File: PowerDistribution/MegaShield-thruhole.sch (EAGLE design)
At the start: 36 parts, among them IC1 TLE5205-2, IC2 TLE5205-2, IC3 TLE5205-2, J10 DCJ0202

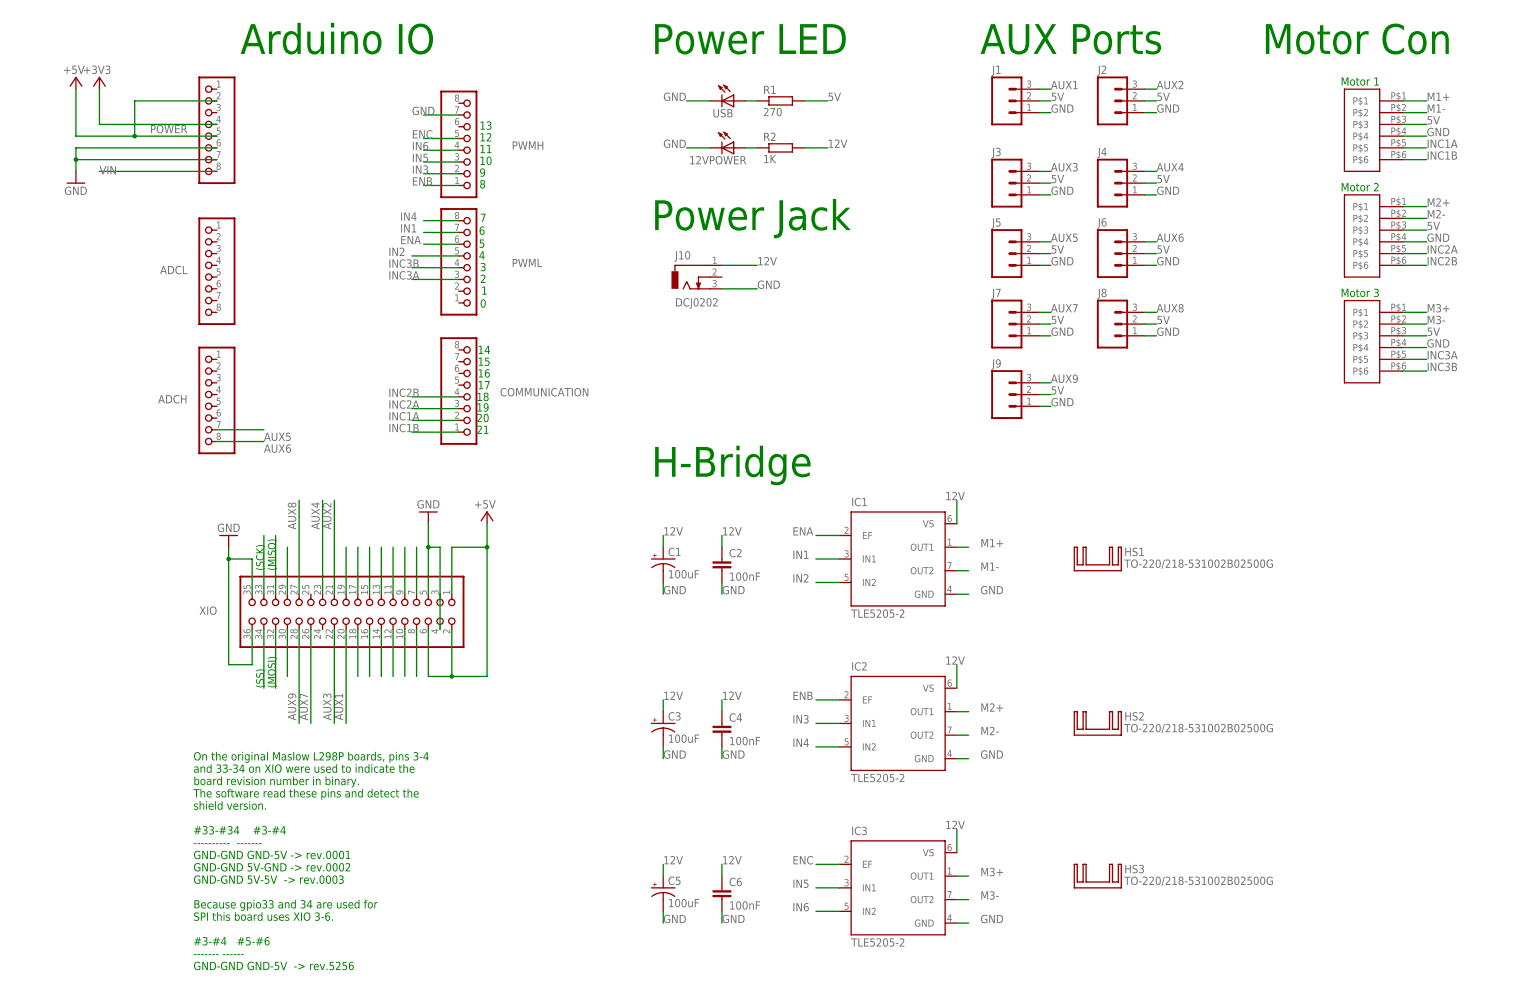
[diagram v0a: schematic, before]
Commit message: clean up and correct pin spacing
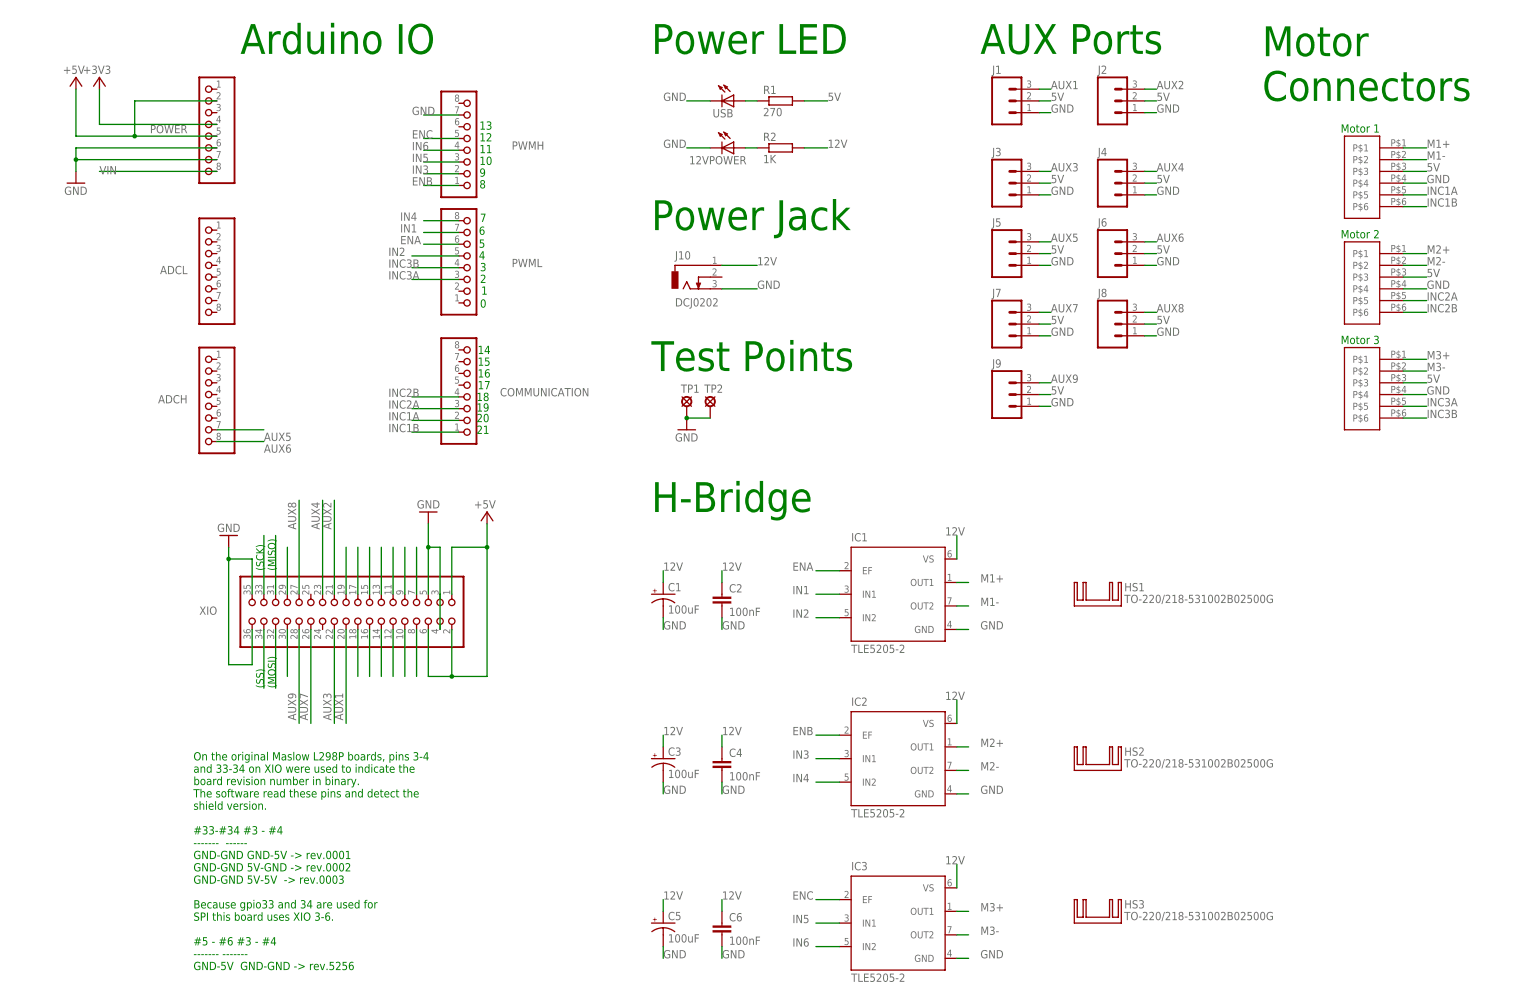
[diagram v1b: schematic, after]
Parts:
- added TP1, TP2: LSP10, solpad:LSP10
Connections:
- net GND: now also TP1.MP, TP2.MP
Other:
- note added: "Motor Connectors"
- note added: "On the original Maslow L298P boards, pins 3-4 and 33-34 on XIO were used to indicate the board revision number in binary. The software read these pins and detect the shield version. #33-#34 #3 - #4 ------- ------ GND-GND GND-5V -> rev.0001 GND-GND 5V-GND -> rev.0002 GND-GND 5V-5V -> rev.0003 Because gpio33 and 34 are used for SPI this board uses XIO 3-6. #5 - #6 #3 - #4 ------- ------- GND-5V GND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"
- note added: "Test Points"
- note removed: "Motor Con"
- note removed: "On the original Maslow L298P boards, pins 3-4 and 33-34 on XIO were used to indicate the board revision number in binary. The software read these pins and detect the shield version. #33-#34 #3-#4 ---------- ------- GND-GND GND-5V -> rev.0001 GND-GND 5V-GND -> rev.0002 GND-GND 5V-5V -> rev.0003 Because gpio33 and 34 are used for SPI this board uses XIO 3-6. #3-#4 #5-#6 ------- ------ GND-GND GND-5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"
- moved on the sheet: C1, C2, C3, C4, C5, C6, HS1, HS2, HS3, IC1, IC2, IC3

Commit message: Move AUX conections to other source pins
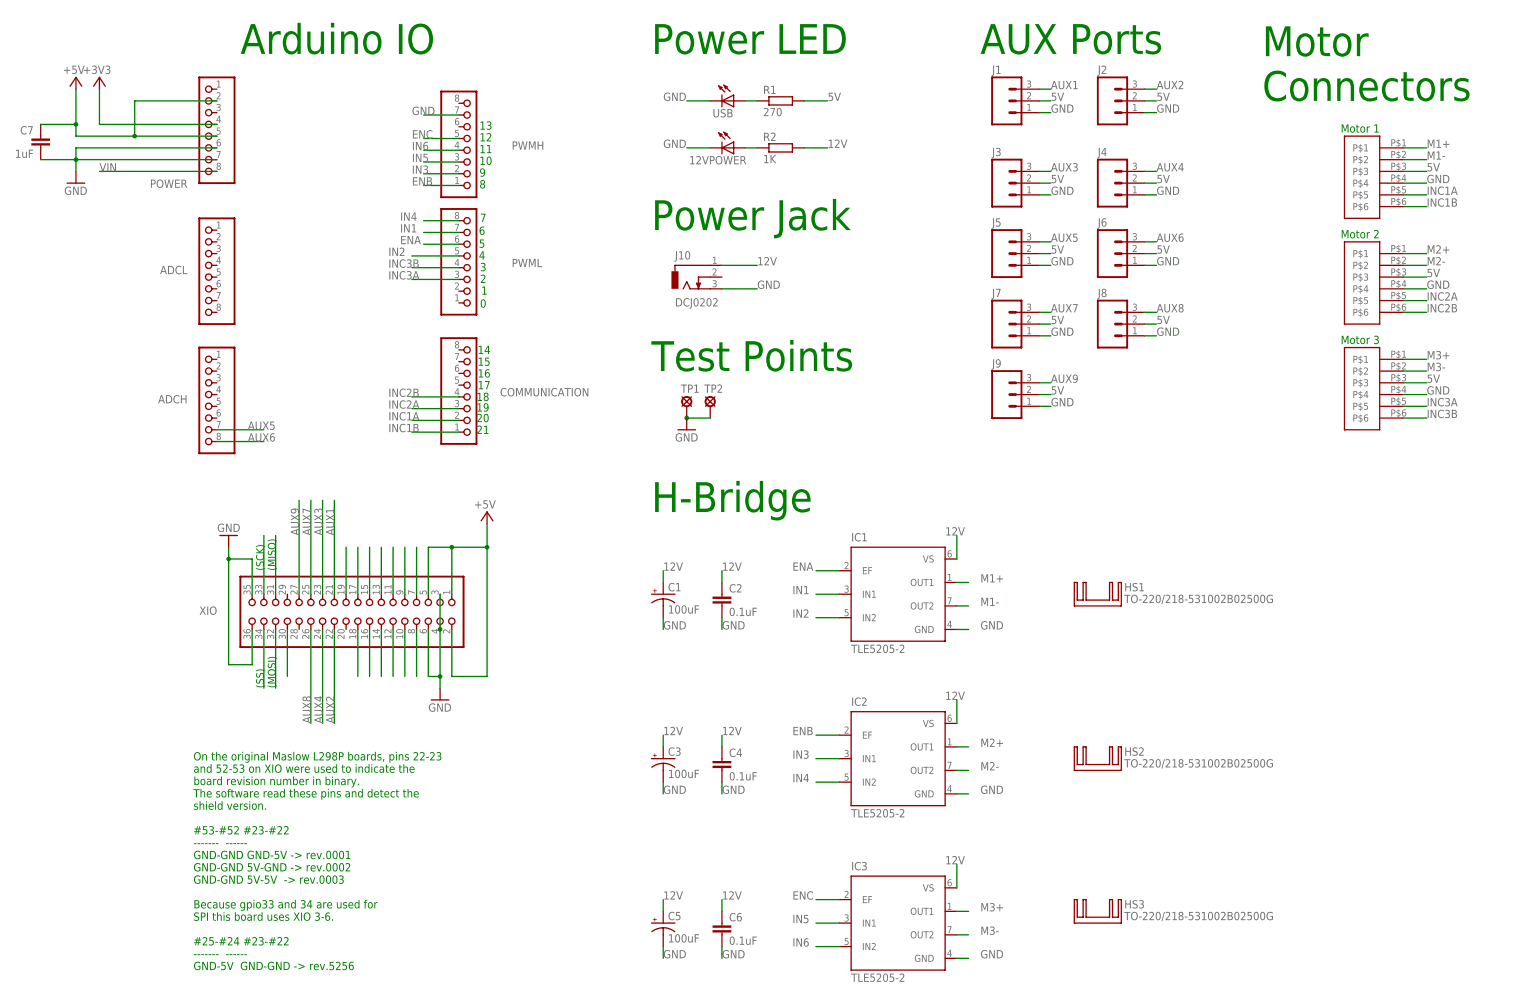
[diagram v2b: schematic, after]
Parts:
- added C7: 1uF, SparkFun:CAPPTH
- C2, C4, C6: value 100nF -> 0.1uF
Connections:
- removed net PL1: XIO.29
- net 5V: now also C7.1, XIO.5; no longer XIO.6
- net AUX1: now also XIO.21; no longer XIO.20
- net AUX2: now also XIO.22; no longer XIO.21
- net AUX3: now also XIO.23; no longer XIO.22
- net AUX4: now also XIO.24; no longer XIO.23
- net AUX7: now also XIO.25; no longer XIO.26
- net AUX8: now also XIO.26; no longer XIO.27
- net AUX9: now also XIO.27; no longer XIO.28
- net GND: now also C7.2, XIO.6; no longer XIO.5
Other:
- note added: "On the original Maslow L298P boards, pins 22-23 and 52-53 on XIO were used to indicate the board revision number in binary. The software read these pins and detect the shield version. #53-#52 #23-#22 ------- ------ GND-GND GND-5V -> rev.0001 GND-GND 5V-GND -> rev.0002 GND-GND 5V-5V -> rev.0003 Because gpio33 and 34 are used for SPI this board uses XIO 3-6. #25-#24 #23-#22 ------- ------ GND-5V GN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"
- note removed: "On the original Maslow L298P boards, pins 3-4 and 33-34 on XIO were used to indicate the board revision number in binary. The software read these pins and detect the shield version. #33-#34 #3 - #4 ------- ------ GND-GND GND-5V -> rev.0001 GND-GND 5V-GND -> rev.0002 GND-GND 5V-5V -> rev.0003 Because gpio33 and 34 are used for SPI this board uses XIO 3-6. #5 - #6 #3 - #4 ------- ------- GND-5V GND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"
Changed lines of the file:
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@@
 <attribute name="DIGIKEY" value="HS351-ND"/>
 </part>
-<part name="C4" library="SparkFun" deviceset="CAP" device="PTH" value="100nF"/>
+<part name="C4" library="SparkFun" deviceset="CAP" device="PTH" value="0.1uF"/>
 <part name="C3" library="SparkFun" deviceset="CAP_POL" device="PTH1" value="100uF"/>
-<part name="C2" library="SparkFun" deviceset="CAP" device="PTH" value="100nF"/>
+<part name="C2" library="SparkFun" deviceset="CAP" device="PTH" value="0.1uF"/>
 <part name="C1" library="SparkFun" deviceset="CAP_POL" device="PTH1" value="100uF"/>
-<part name="C6" library="SparkFun" deviceset="CAP" device="PTH" value="100nF"/>
+<part name="C6" library="SparkFun" deviceset="CAP" device="PTH" value="0.1uF"/>
 <part name="C5" library="SparkFun" deviceset="CAP_POL" device="PTH1" value="100uF"/>
 <part name="XIO" library="SmartPrj" deviceset="PINHD-2X18" device="" value="18x2F-H8.5"/>
@@
 <part name="TP2" library="solpad" library_urn="urn:adsk.eagle:library:364" deviceset="LSP10" device="" package3d_urn="urn:adsk.eagle:package:26501/1"/>
 <part name="GND2" library="supply1" deviceset="GND" device=""/>
+<part name="C7" library="SparkFun" deviceset="CAP" device="PTH" value="1uF"/>
 </parts>
 <sheets>
@@
 Connectors</text>
 <text x="309.88" y="195.58" size="1.778" layer="91" rot="R180">Motor 3</text>
-<text x="53.34" y="58.42" size="1.778" layer="91">On the original Maslow L298P boards, pins 3-4
-and 33-34 on XIO were used to indicate the
+<text x="53.34" y="58.42" size="1.778" layer="91">On the original Maslow L298P boards, pins 22-23
+and 52-53 on XIO were used to indicate the
 board revision number in binary.
 The software read these pins and detect the
 shield version.
-#33-#34 #3 - #4
+#53-#52 #23-#22
 -------  ------
 GND-GND GND-5V -&gt; rev.0001
@@
 Because gpio33 and 34 are used for
 SPI this board uses XIO 3-6.
-#5 - #6 #3 - #4
-------- -------
+#25-#24 #23-#22
+-------  ------
 GND-5V  GND-GND -&gt; rev.5256
 </text>
@@
 </instance>
 <instance part="POWER" gate="A" x="55.88" y="238.76" smashed="yes" rot="MR0">
-<attribute name="NAME" x="52.07" y="239.395" size="1.778" layer="95" rot="MR0"/>
-</instance>
-<instance part="GND1" gate="1" x="104.14" y="157.48" smashed="yes" rot="R180">
-<attribute name="VALUE" x="106.68" y="160.02" size="1.778" layer="96" rot="R180"/>
+<attribute name="NAME" x="52.07" y="227.584" size="1.778" layer="95" rot="MR0"/>
+</instance>
+<instance part="GND1" gate="1" x="106.68" y="116.84" smashed="yes">
+<attribute name="VALUE" x="104.14" y="114.3" size="1.778" layer="96"/>
 </instance>
 <instance part="TP1" gate="1" x="160.02" y="180.34"/>
@@
 <attribute name="VALUE" x="157.48" y="172.72" size="1.778" layer="96"/>
 </instance>
+<instance part="C7" gate="G$1" x="20.32" y="236.22" rot="MR0"/>
 </instances>
 <busses>
@@
 <pinref part="POWER" gate="A" pin="6"/>
 <pinref part="POWER" gate="A" pin="7"/>
+<pinref part="C7" gate="G$1" pin="2"/>
+<wire x1="27.94" y1="233.68" x2="20.32" y2="233.68" width="0.1524" layer="91"/>
 </segment>
 <segment>
@@
 <wire x1="110.744" y1="243.332" x2="103.124" y2="243.332" width="0.1524" layer="91"/>
 <label x="100.584" y="243.332" size="1.778" layer="95"/>
-</segment>
-<segment>
-<pinref part="XIO" gate="A" pin="5"/>
-<wire x1="104.14" y1="139.7" x2="104.14" y2="149.86" width="0.1524" layer="91"/>
-<wire x1="104.14" y1="149.86" x2="106.68" y2="149.86" width="0.1524" layer="91"/>
-<pinref part="XIO" gate="A" pin="3"/>
-<wire x1="106.68" y1="149.86" x2="106.68" y2="139.7" width="0.1524" layer="91"/>
-<pinref part="XIO" gate="A" pin="4"/>
-<wire x1="106.68" y1="139.7" x2="106.68" y2="132.08" width="0.1524" layer="91"/>
-<pinref part="GND1" gate="1" pin="GND"/>
-<wire x1="104.14" y1="154.94" x2="104.14" y2="149.86" width="0.1524" layer="91"/>
-<junction x="104.14" y="149.86"/>
 </segment>
 <segment>
@@
 <wire x1="165.1" y1="177.8" x2="160.02" y2="177.8" width="0.1524" layer="91"/>
 <junction x="160.02" y="177.8"/>
+</segment>
+<segment>
+<pinref part="XIO" gate="A" pin="3"/>
+<pinref part="XIO" gate="A" pin="4"/>
+<wire x1="106.68" y1="139.7" x2="106.68" y2="132.08" width="0.1524" layer="91"/>
+<pinref part="GND1" gate="1" pin="GND"/>
+<wire x1="106.68" y1="119.38" x2="106.68" y2="121.92" width="0.1524" layer="91"/>
+<wire x1="106.68" y1="132.08" x2="106.68" y2="121.92" width="0.1524" layer="91"/>
+<wire x1="106.68" y1="121.92" x2="104.14" y2="121.92" width="0.1524" layer="91"/>
+<pinref part="XIO" gate="A" pin="6"/>
+<wire x1="104.14" y1="121.92" x2="104.14" y2="132.08" width="0.1524" layer="91"/>
+<junction x="106.68" y="121.92"/>
+<junction x="106.68" y="132.08"/>
 </segment>
 </net>
@@
 <pinref part="XIO" gate="A" pin="1"/>
 <pinref part="5V" gate="1" pin="+5V"/>
-<wire x1="104.14" y1="132.08" x2="104.14" y2="121.92" width="0.1524" layer="91"/>
-<pinref part="XIO" gate="A" pin="6"/>
-<wire x1="104.14" y1="121.92" x2="109.22" y2="121.92" width="0.1524" layer="91"/>
-<junction x="109.22" y="121.92"/>
+<pinref part="XIO" gate="A" pin="5"/>
+<wire x1="104.14" y1="139.7" x2="104.14" y2="149.86" width="0.1524" layer="91"/>
+<wire x1="104.14" y1="149.86" x2="109.22" y2="149.86" width="0.1524" layer="91"/>
+<junction x="109.22" y="149.86"/>
 </segment>
 <segment>
@@
 </segment>
 <segment>
-<wire x1="27.94" y1="238.76" x2="27.94" y2="248.92" width="0.1524" layer="91"/>
+<wire x1="27.94" y1="238.76" x2="27.94" y2="241.3" width="0.1524" layer="91"/>
+<wire x1="27.94" y1="241.3" x2="27.94" y2="248.92" width="0.1524" layer="91"/>
 <wire x1="58.42" y1="238.76" x2="40.64" y2="238.76" width="0.1524" layer="91"/>
 <wire x1="40.64" y1="238.76" x2="27.94" y2="238.76" width="0.1524" layer="91"/>
@@
 <pinref part="POWER" gate="A" pin="5"/>
 <pinref part="POWER" gate="A" pin="2"/>
+<pinref part="C7" gate="G$1" pin="1"/>
+<wire x1="27.94" y1="241.3" x2="20.32" y2="241.3" width="0.1524" layer="91"/>
+<junction x="27.94" y="241.3"/>
 </segment>
 </net>
@@
 </segment>
 <segment>
-<wire x1="83.82" y1="132.08" x2="83.82" y2="111.76" width="0.1524" layer="91"/>
-<label x="83.185" y="112.395" size="1.778" layer="95" rot="R90"/>
-<pinref part="XIO" gate="A" pin="22"/>
+<wire x1="81.28" y1="160.02" x2="81.28" y2="139.7" width="0.1524" layer="91"/>
+<label x="81.28" y="152.4" size="1.778" layer="95" rot="R90"/>
+<pinref part="XIO" gate="A" pin="23"/>
 </segment>
 </net>
@@
 </segment>
 <segment>
-<wire x1="86.36" y1="132.08" x2="86.36" y2="111.76" width="0.1524" layer="91"/>
-<label x="85.725" y="112.395" size="1.778" layer="95" rot="R90"/>
-<pinref part="XIO" gate="A" pin="20"/>
+<wire x1="83.82" y1="139.7" x2="83.82" y2="160.02" width="0.1524" layer="91"/>
+<label x="83.82" y="152.4" size="1.778" layer="95" rot="R90"/>
+<pinref part="XIO" gate="A" pin="21"/>
 </segment>
 </net>
@@
 </segment>
 <segment>
-<wire x1="83.82" y1="139.7" x2="83.82" y2="160.02" width="0.1524" layer="91"/>
-<label x="83.185" y="153.67" size="1.778" layer="95" rot="R90"/>
-<pinref part="XIO" gate="A" pin="21"/>
+<wire x1="83.82" y1="132.08" x2="83.82" y2="111.76" width="0.1524" layer="91"/>
+<label x="83.82" y="111.76" size="1.778" layer="95" rot="R90"/>
+<pinref part="XIO" gate="A" pin="22"/>
 </segment>
 </net>
@@
 </segment>
 <segment>
-<wire x1="81.28" y1="160.02" x2="81.28" y2="139.7" width="0.1524" layer="91"/>
-<label x="80.645" y="153.67" size="1.778" layer="95" rot="R90"/>
-<pinref part="XIO" gate="A" pin="23"/>
+<pinref part="XIO" gate="A" pin="24"/>
+<wire x1="81.28" y1="132.08" x2="81.28" y2="111.76" width="0.1524" layer="91"/>
+<label x="81.28" y="111.76" size="1.778" layer="95" rot="R90"/>
 </segment>
 </net>
@@
 <segment>
 <wire x1="68.58" y1="175.26" x2="58.42" y2="175.26" width="0.1524" layer="91"/>
-<label x="68.58" y="174.625" size="1.778" layer="95" rot="MR180"/>
+<label x="71.12" y="175.26" size="1.778" layer="95" rot="MR0"/>
 <pinref part="ADCH" gate="A" pin="7"/>
 </segment>
@@
 <segment>
 <wire x1="58.42" y1="172.72" x2="68.58" y2="172.72" width="0.1524" layer="91"/>
-<label x="68.58" y="172.085" size="1.778" layer="95" rot="MR180"/>
+<label x="71.12" y="172.72" size="1.778" layer="95" rot="MR0"/>
 <pinref part="ADCH" gate="A" pin="8"/>
 </segment>
@@
 </segment>
 </net>
-<net name="PL1" class="0">
-<segment>
-<wire x1="73.66" y1="139.7" x2="73.66" y2="149.86" width="0.1524" layer="91"/>
-<pinref part="XIO" gate="A" pin="29"/>
-</segment>
-</net>
 <net name="AUX7" class="0">
 <segment>
@@
 </segment>
 <segment>
-<wire x1="78.74" y1="132.08" x2="78.74" y2="111.76" width="0.1524" layer="91"/>
-<label x="78.105" y="112.395" size="1.778" layer="95" rot="R90"/>
-<pinref part="XIO" gate="A" pin="26"/>
+<pinref part="XIO" gate="A" pin="25"/>
+<wire x1="78.74" y1="139.7" x2="78.74" y2="160.02" width="0.1524" layer="91"/>
+<label x="78.74" y="152.4" size="1.778" layer="95" rot="R90"/>
 </segment>
 </net>
@@
 </segment>
 <segment>
-<wire x1="76.2" y1="139.7" x2="76.2" y2="160.02" width="0.1524" layer="91"/>
-<label x="75.565" y="153.67" size="1.778" layer="95" rot="R90"/>
-<pinref part="XIO" gate="A" pin="27"/>
+<pinref part="XIO" gate="A" pin="26"/>
+<wire x1="78.74" y1="132.08" x2="78.74" y2="111.76" width="0.1524" layer="91"/>
+<label x="78.74" y="111.76" size="1.778" layer="95" rot="R90"/>
 </segment>
 </net>
@@
 </segment>
 <segment>
-<wire x1="76.2" y1="111.76" x2="76.2" y2="132.08" width="0.1524" layer="91"/>
-<label x="75.565" y="112.395" size="1.778" layer="95" rot="R90"/>
-<pinref part="XIO" gate="A" pin="28"/>
+<wire x1="76.2" y1="139.7" x2="76.2" y2="160.02" width="0.1524" layer="91"/>
+<label x="76.2" y="152.4" size="1.778" layer="95" rot="R90"/>
+<pinref part="XIO" gate="A" pin="27"/>
 </segment>
 </net>
@@
 <segment>
 <wire x1="33.02" y1="231.14" x2="58.42" y2="231.14" width="0.1524" layer="91"/>
-<label x="33.02" y="230.505" size="1.778" layer="95"/>
+<label x="33.02" y="231.14" size="1.778" layer="95"/>
 <pinref part="POWER" gate="A" pin="8"/>
 </segment>
